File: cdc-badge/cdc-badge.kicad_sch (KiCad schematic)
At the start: 149 parts, among them J1 USB_C, J2 JST S2B-PH-SM4-TB, J3 Conn_02x20_Odd_Even, J4 Conn_Grove, J5 Conn_02x03_Odd_Even, J6 Conn_01x06, J7 Conn_01x24, Q1 Si1308EDL, Q2 Si1308EDL, SW0 0, SW1 1, SW10 YES, SW11 NO, SW12 power on/reset, SW13 reset, SW14 flash/power off, SW15 MST-22D18G2 3J, SW16 MST-22D18G2 3J, SW2 2, SW3 3, SW4 4, SW5 5, SW6 6, SW7 7, SW8 8, SW9 9, U1 ESP32-S3-WROOM-1-N16R8, U2 TCA9535PWR, U3 TROPIC01, U4 TPS613222ADBV, U6 BQ25895RTW, U7 USBLC6-2SC6, U8 TLV62569DBV

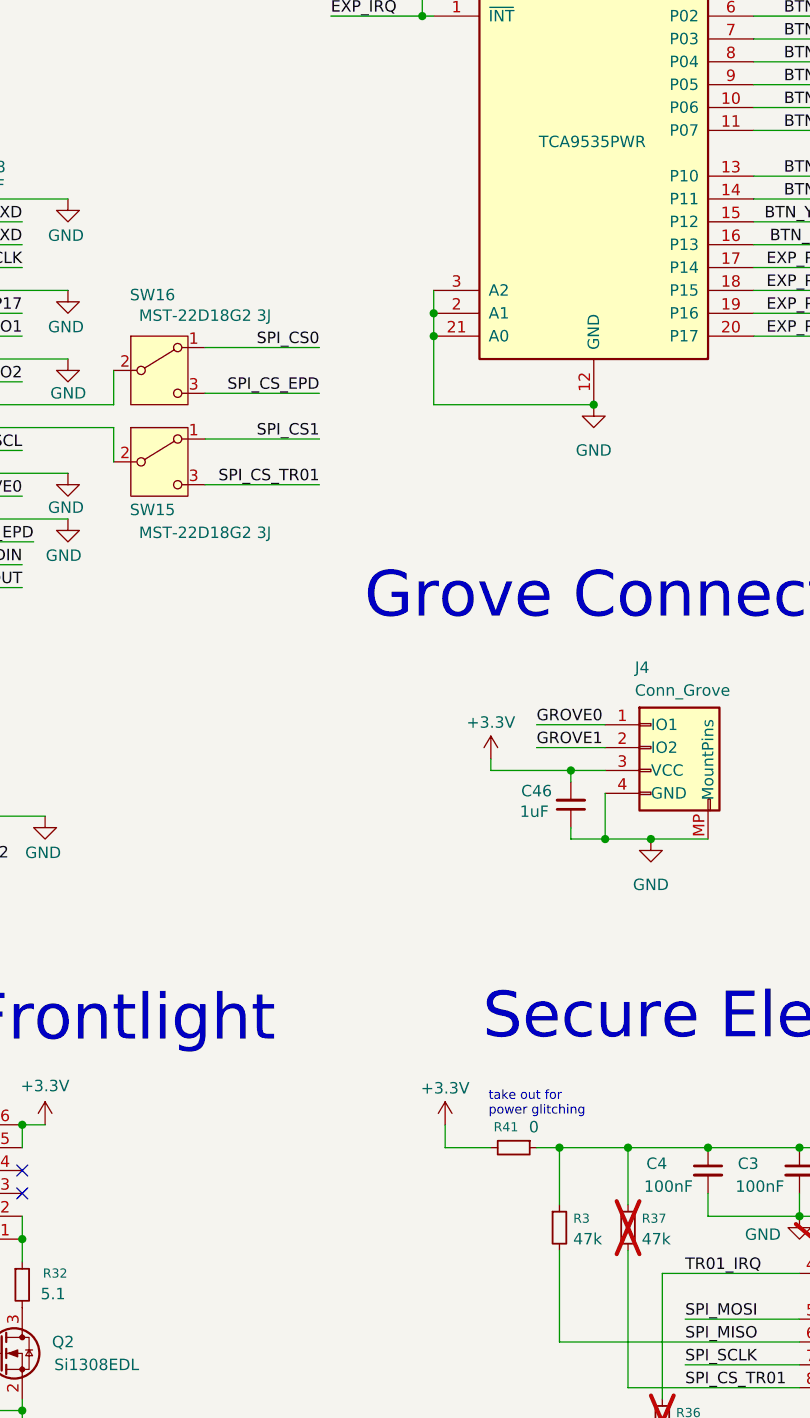
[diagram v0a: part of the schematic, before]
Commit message: schematic: ceetee reviews, add pull-ups to all SPI CS
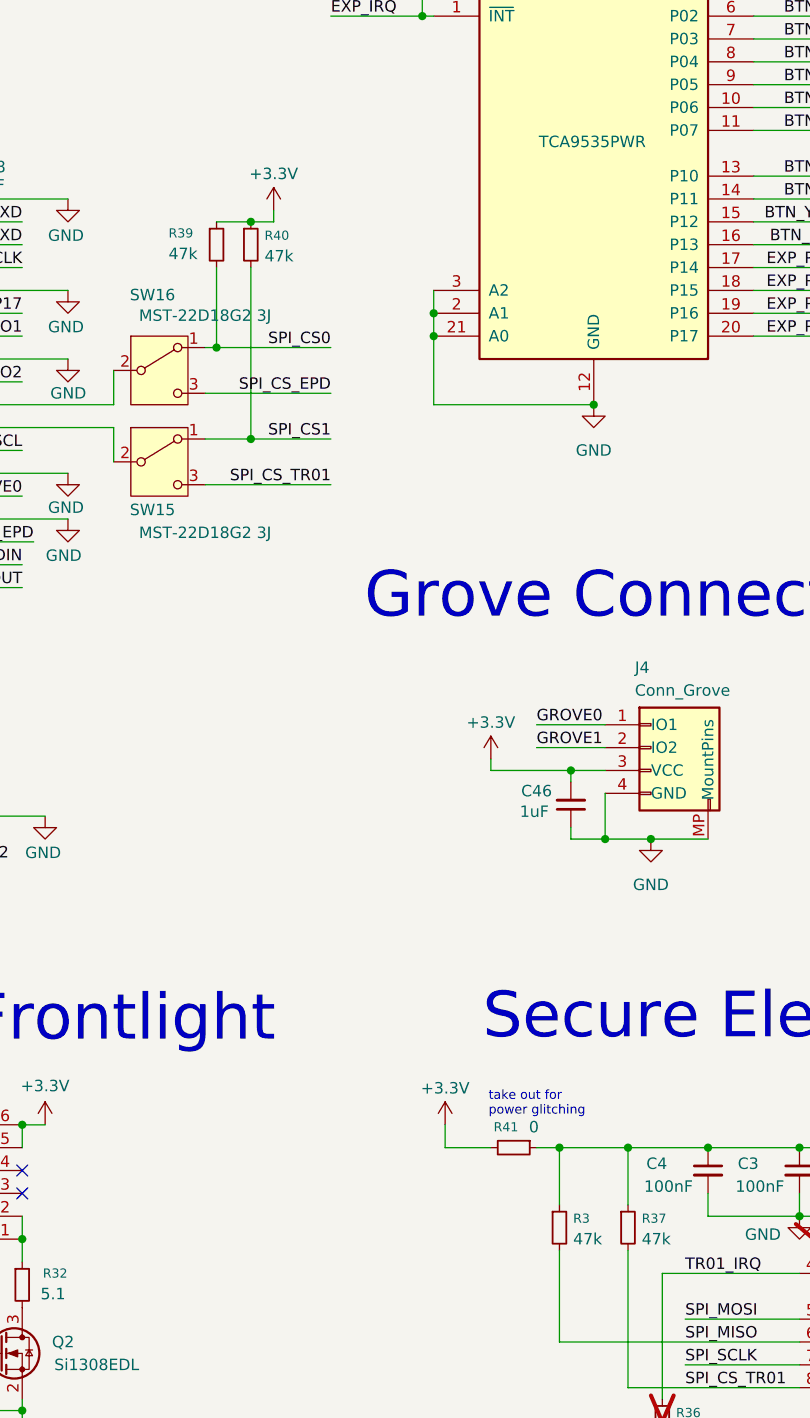
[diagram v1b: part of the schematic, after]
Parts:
- added R39, R40: 47k, Resistor_SMD:R_0603_1608Metric, symbol Device:R_Small
- R37: now fitted
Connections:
- net +3.3V: now also R39.1, R40.1
- net SPI_CS0: now also R39.2
- net SPI_CS1: now also R40.2

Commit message: pcb: relax ESP32 keep-out zone, import from schematic
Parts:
- U1: footprint RF_Module:ESP32-S3-WROOM-1 -> CDC_Badge:ESP32-S3-WROOM-1
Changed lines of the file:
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@@
 			)
 		)
-		(property "Footprint" "RF_Module:ESP32-S3-WROOM-1"
+		(property "Footprint" "CDC_Badge:ESP32-S3-WROOM-1"
 			(at 73.66 163.83 0)
 			(effects

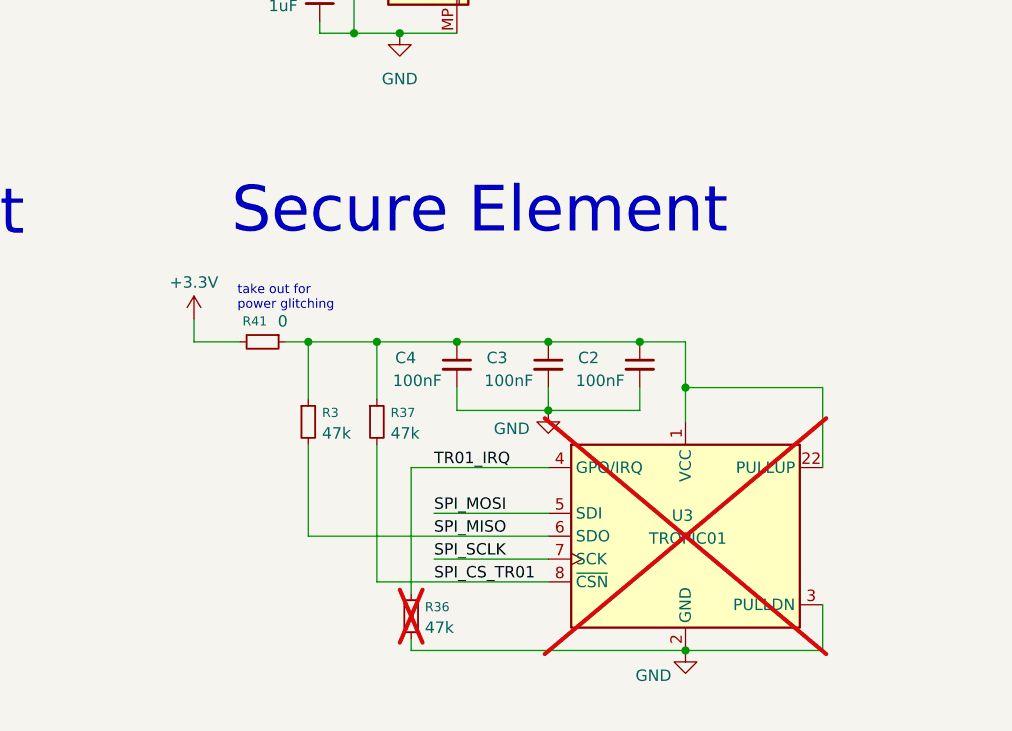
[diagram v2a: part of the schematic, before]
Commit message: schematic: TROPIC01 symbol now adheres to library conventions
https://klc.kicad.org/symbol/s4/s4.3.html
As there are decoupling capacitors on each VCC pin they must be
separated.

https://klc.kicad.org/symbol/s4/s4.6.html
Hidden pins contained within the symbol.
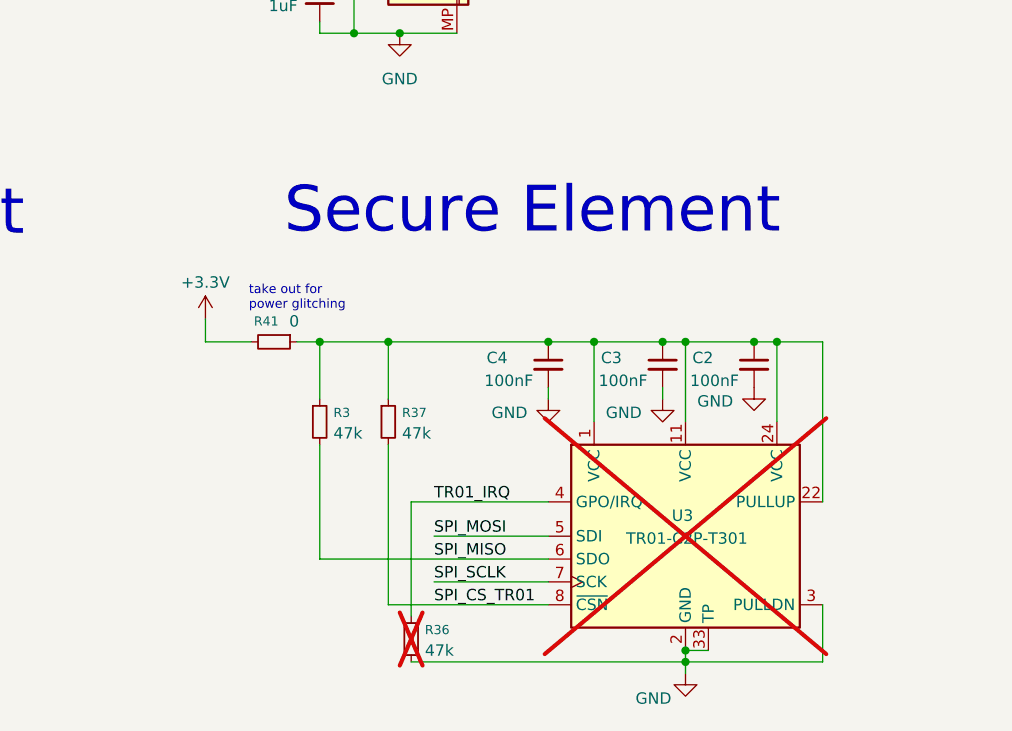
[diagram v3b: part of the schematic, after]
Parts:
- U3: value TROPIC01 -> TR01-C2P-T301
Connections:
- net GND: now also U3.33 (TP)
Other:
- moved on the sheet: C2, C3, C4, R3, R36, R37, R41

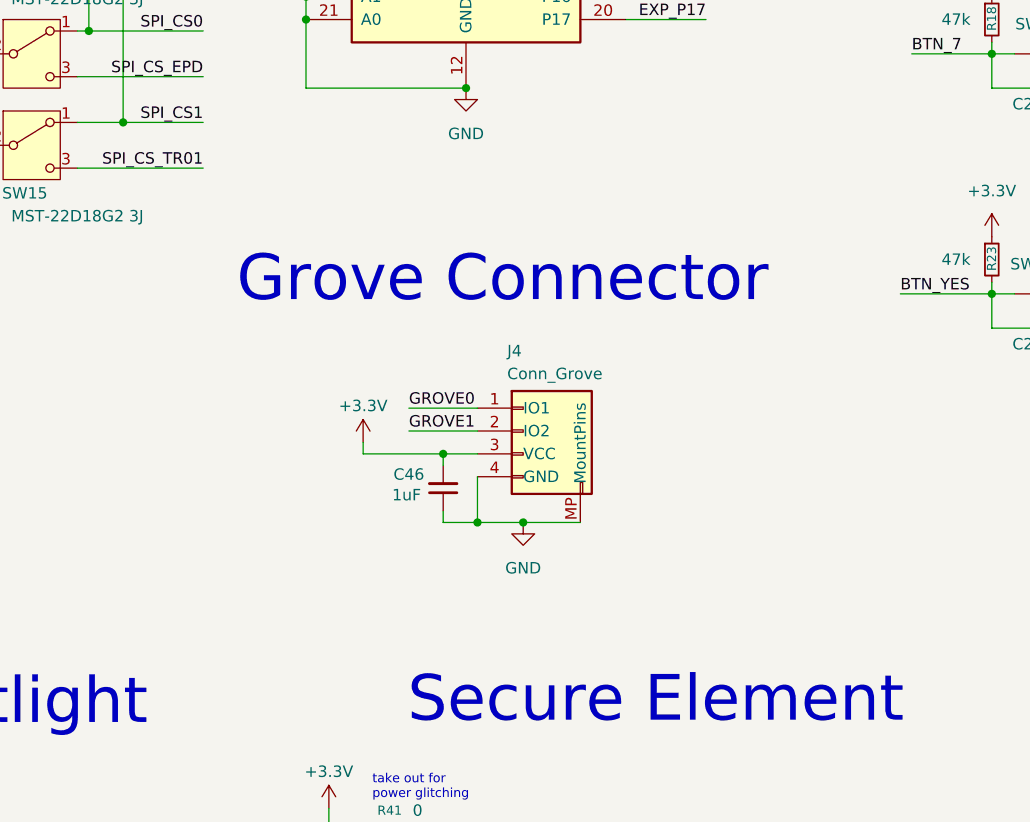
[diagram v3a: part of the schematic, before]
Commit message: schematic: ceetee reviews, Grove connector
Add selectable output voltage with a switch.
Add optional pull-ups for I2C.
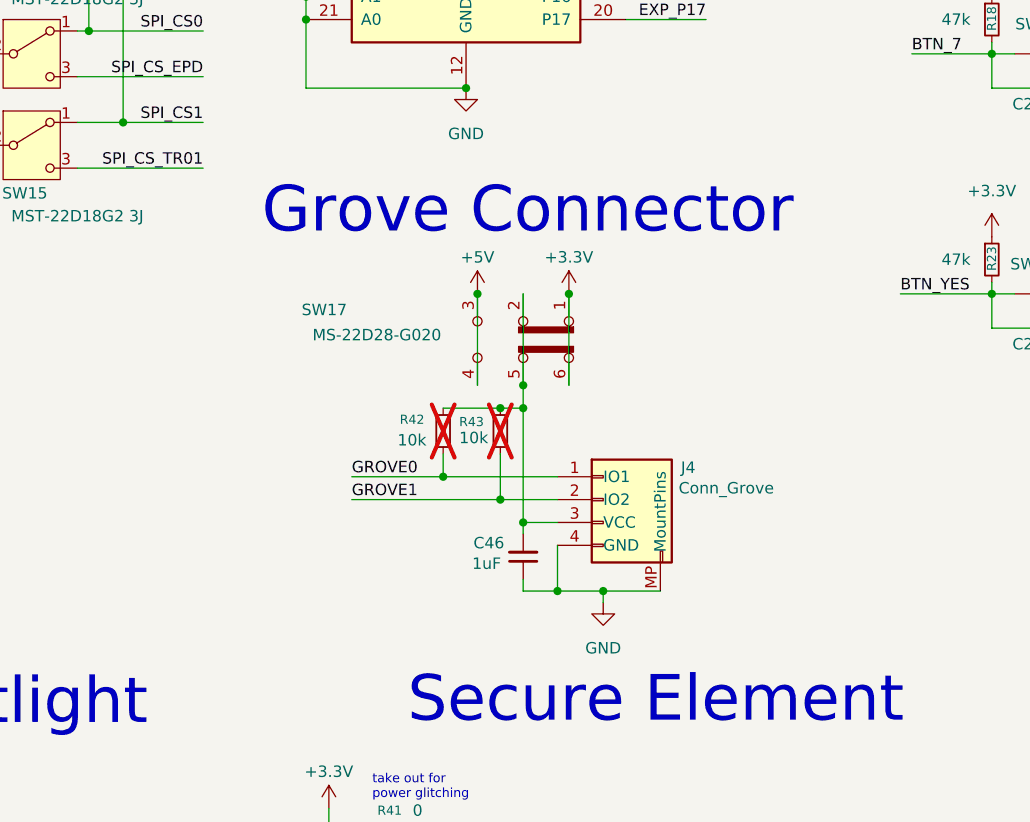
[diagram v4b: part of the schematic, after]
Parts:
- added R42, R43: 10k, Resistor_SMD:R_0603_1608Metric, symbol Device:R_Small
- added SW17: MS-22D28-G020, CDC_Badge:SW_DPDT_G-Switch_MS-22D28-G020, symbol Switch:SW_Slide_DPDT
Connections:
- net +3.3V: now also SW17.1 (A), SW17.6 (C); no longer C46.2, J4.3 (VCC)
- net +5V: now also SW17.3 (C), SW17.4 (A)
- net GROVE0: now also R42.1
- net GROVE1: now also R43.1
- new net: C46.2, J4.3 (VCC), R42.2, R43.2, SW17.2 (B), SW17.5 (B)
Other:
- moved on the sheet: C46, J4

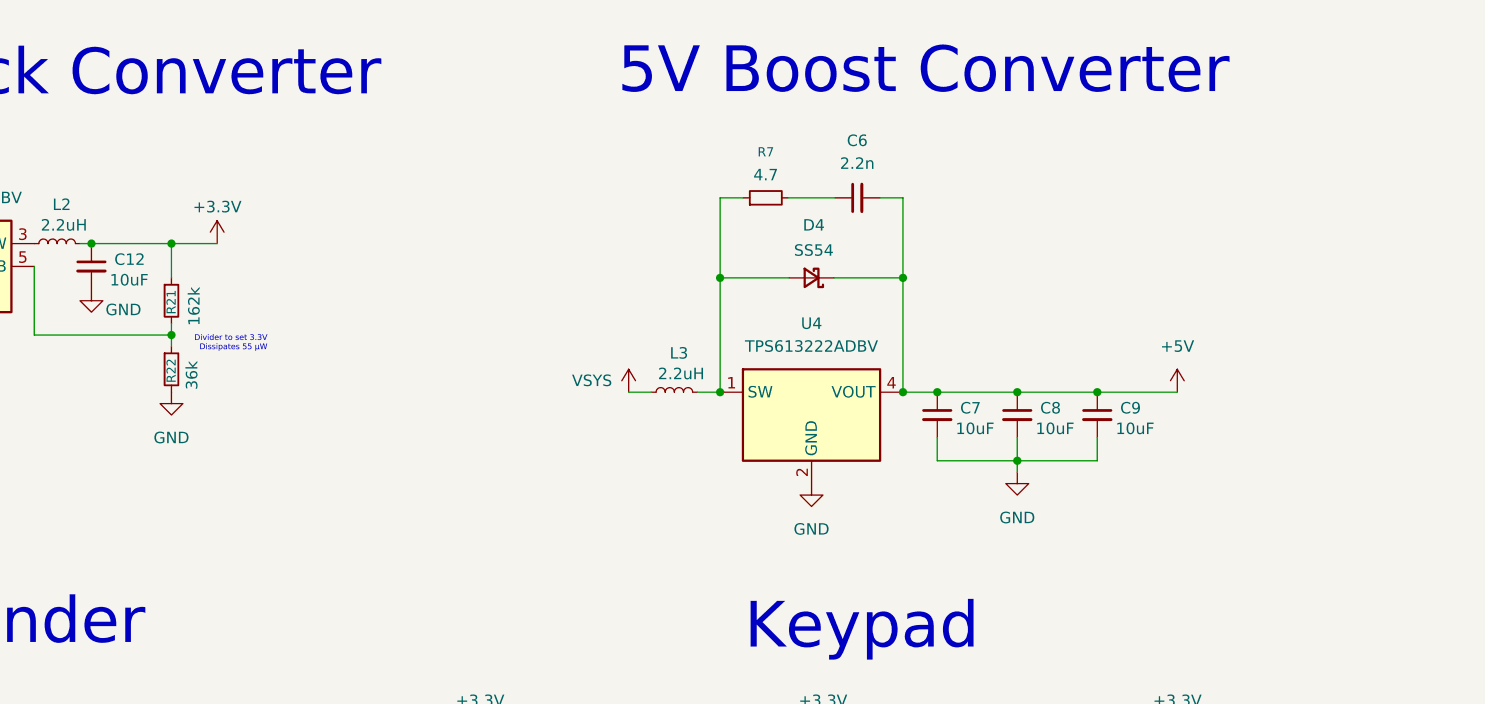
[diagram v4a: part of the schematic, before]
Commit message: schematic: ceetee reviews, replace boost converter
Now using the TLV61070ADBVR instead of the TPS613222A because it does
not need an external compensation network.
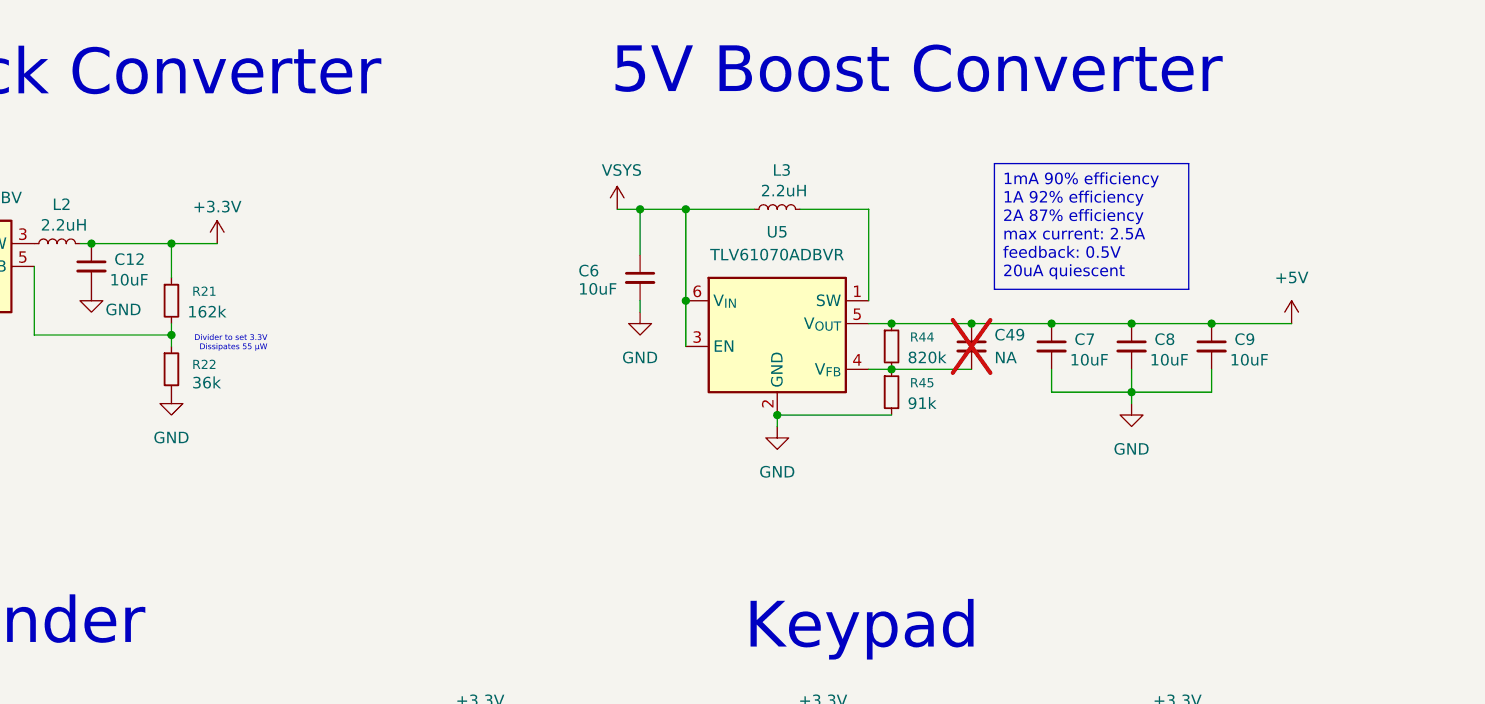
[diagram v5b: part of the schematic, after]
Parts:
- removed D4: SS54, Diode_SMD:D_SMA, symbol Device:D_Schottky_Small
- removed R7: 4.7, Resistor_SMD:R_0603_1608Metric, symbol Device:R_Small
- removed U4: TPS613222ADBV, Package_TO_SOT_SMD:SOT-23-5, symbol Regulator_Switching:TPS613222ADBV
- added C49: NA, Capacitor_SMD:C_0603_1608Metric, symbol Device:C_Small
- added R44: 820k, Resistor_SMD:R_0603_1608Metric, symbol Device:R_Small
- added R45: 91k, Resistor_SMD:R_0603_1608Metric, symbol Device:R_Small
- added U5: TLV61070ADBVR, Package_TO_SOT_SMD:SOT-23-6, symbol Regulator_Switching:TLV61070ADBV
- C6: value 2.2n -> 10uF; footprint Capacitor_SMD:C_0603_1608Metric -> Capacitor_SMD:C_0805_2012Metric; JLCPCB PN C1604 -> C15850
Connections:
- net +5V: now also C49.1, R44.1, U5.5 (V_{OUT}); no longer C6.2
- net GND: now also C6.2, R45.2, U5.2 (GND)
- net VSYS: now also C6.1, U5.3 (EN), U5.6 (V_{IN})
- net at L3.2: now also U5.1 (SW)
- new net: C49.2, R44.2, R45.1, U5.4 (V_{FB})
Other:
- moved on the sheet: C7, C8, C9, L3

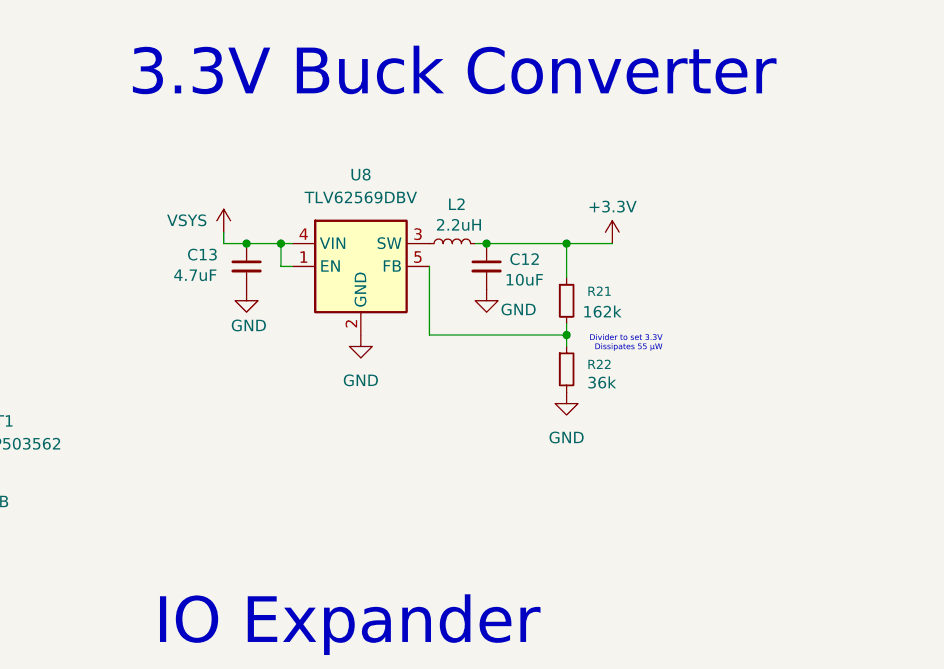
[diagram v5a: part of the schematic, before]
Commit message: schematic: ceetee reviews, buck converter
Use more common resistor values in the voltage divider.
Add optional feed forward capacitor.
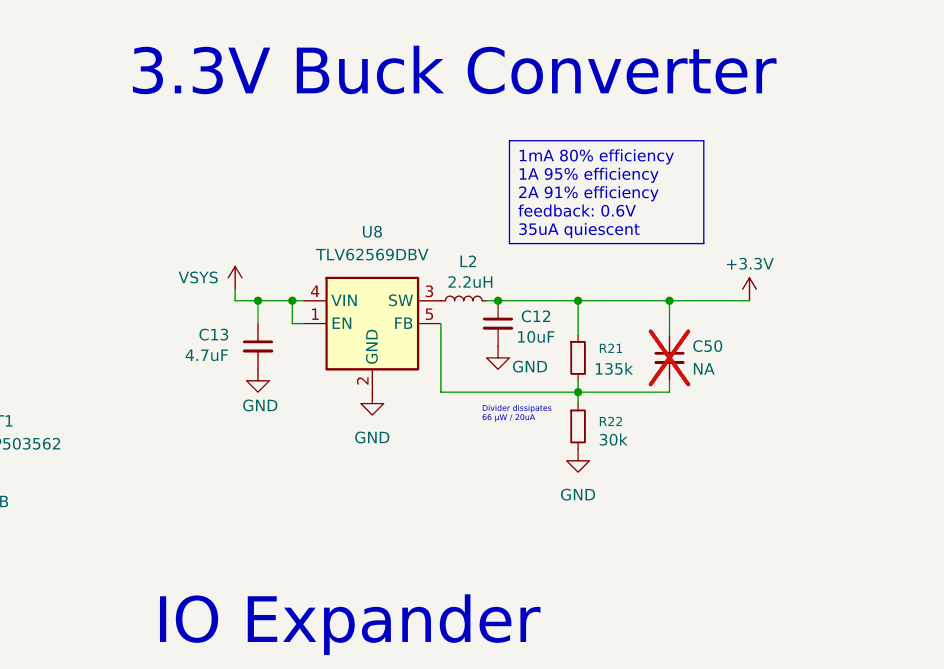
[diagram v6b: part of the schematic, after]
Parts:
- added C50: NA, Capacitor_SMD:C_0603_1608Metric, symbol Device:C_Small
- R21: value 162k -> 135k; JLCPCB PN C22815 -> C861113; MPN (none) -> RT0603BRD07135KL
- R22: value 36k -> 30k; JLCPCB PN C23147 -> C22984; MPN (none) -> 0603WAF3002T5E
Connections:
- net +3.3V: now also C50.1
- net at R21.2, R22.1, U8.5 (FB): now also C50.2
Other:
- note added: "Divider dissipates 66 µW / 20uA"
- note removed: "Divider to set 3.3V Dissipates 55 µW"
- moved on the sheet: C12, C13, L2, R21, R22, U8
